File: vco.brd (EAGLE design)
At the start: 100 x 80 mm, 24 parts, among them IC2 CEM3340

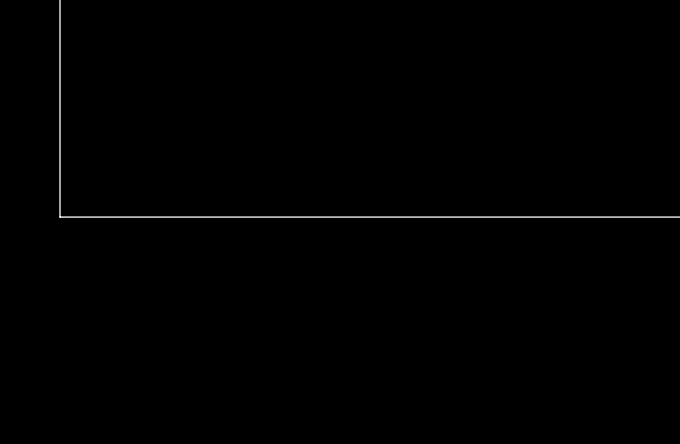
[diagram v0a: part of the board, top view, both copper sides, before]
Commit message: Added -5v regulator as option. fixed pin 4.
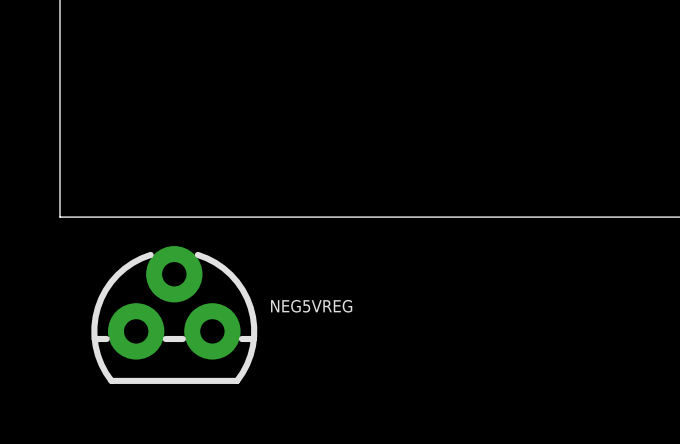
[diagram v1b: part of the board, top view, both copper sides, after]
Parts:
- added NEG5VREG: (no value), SparkFun-IC-Power:TO-92
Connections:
- removed net N$14: IC2.4, R10.1, R11.1, R12.2, R13.2, R13.3
- new net -12V: NEG5VREG.3, R10.1, R11.1, R13.2, R13.3
- new net N$18: IC2.4, R12.2
- net PE: now also NEG5VREG.2
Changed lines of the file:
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@@
 </element>
 <element name="J1" library="SparkFun-Connectors" package="2X8-SHROUDED_LOCK" value="" x="78.74" y="59.69" smashed="yes"/>
+<element name="NEG5VREG" library="SparkFun-IC-Power" package="TO-92" value="" x="3.81" y="-3.81" smashed="yes">
+<attribute name="NAME" x="6.985" y="-3.175" size="0.4064" layer="25" ratio="10"/>
+<attribute name="VALUE" x="6.985" y="-5.08" size="0.4064" layer="27" ratio="10"/>
+</element>
 </elements>
 <signals>
@@
 <contactref element="R14" pad="3"/>
 <contactref element="R12" pad="1"/>
-<wire x1="26.67" y1="36.83" x2="16.51" y2="25.4" width="0" layer="19" extent="1-1"/>
-<wire x1="33.02" y1="31.75" x2="26.67" y2="36.83" width="0" layer="19" extent="1-1"/>
-<wire x1="40.64" y1="44.45" x2="33.02" y2="31.75" width="0" layer="19" extent="1-1"/>
-<wire x1="83.82" y1="31.72" x2="26.67" y2="36.83" width="0" layer="19" extent="1-1"/>
+<contactref element="NEG5VREG" pad="2"/>
+<wire x1="40.64" y1="44.45" x2="83.82" y2="31.72" width="0" layer="19" extent="1-1"/>
+<wire x1="33.02" y1="31.75" x2="40.64" y2="44.45" width="0" layer="19" extent="1-1"/>
+<wire x1="26.67" y1="36.83" x2="33.02" y2="31.75" width="0" layer="19" extent="1-1"/>
+<wire x1="16.51" y1="25.4" x2="26.67" y2="36.83" width="0" layer="19" extent="1-1"/>
 <wire x1="34.29" y1="63.5" x2="40.64" y2="44.45" width="0" layer="19" extent="1-1"/>
-<wire x1="3.81" y1="68.58" x2="83.82" y2="31.72" width="0" layer="19" extent="1-1"/>
+<wire x1="3.81" y1="-1.905" x2="16.51" y2="25.4" width="0" layer="19" extent="1-1"/>
+<wire x1="3.81" y1="68.58" x2="34.29" y2="63.5" width="0" layer="19" extent="1-1"/>
 </signal>
 <signal name="N$10">
@@
 <contactref element="R13" pad="1"/>
 <wire x1="78.74" y1="18.99" x2="34.29" y2="68.58" width="0" layer="19" extent="1-1"/>
-</signal>
-<signal name="N$14">
-<contactref element="R13" pad="2"/>
-<contactref element="R10" pad="1"/>
-<contactref element="R13" pad="3"/>
-<contactref element="R11" pad="1"/>
-<contactref element="IC2" pad="4"/>
-<contactref element="R12" pad="2"/>
-<wire x1="83.82" y1="18.99" x2="30.48" y2="24.13" width="0" layer="19" extent="1-1"/>
-<wire x1="81.28" y1="18.99" x2="83.82" y2="18.99" width="0" layer="19" extent="1-1"/>
-<wire x1="24.13" y1="68.58" x2="81.28" y2="18.99" width="0" layer="19" extent="1-1"/>
-<wire x1="13.97" y1="68.58" x2="24.13" y2="68.58" width="0" layer="19" extent="1-1"/>
-<wire x1="11.43" y1="68.58" x2="13.97" y2="68.58" width="0" layer="19" extent="1-1"/>
 </signal>
 <signal name="N$8">
@@
 <wire x1="30.48" y1="44.45" x2="35.56" y2="31.75" width="0" layer="19" extent="1-1"/>
 </signal>
+<signal name="N$18">
+<contactref element="IC2" pad="4"/>
+<contactref element="R12" pad="2"/>
+<wire x1="30.48" y1="24.13" x2="11.43" y2="68.58" width="0" layer="19" extent="1-1"/>
+</signal>
+<signal name="-12V">
+<contactref element="R13" pad="2"/>
+<contactref element="R10" pad="1"/>
+<contactref element="R13" pad="3"/>
+<contactref element="R11" pad="1"/>
+<contactref element="NEG5VREG" pad="3"/>
+<wire x1="81.28" y1="18.99" x2="83.82" y2="18.99" width="0" layer="19" extent="1-1"/>
+<wire x1="24.13" y1="68.58" x2="81.28" y2="18.99" width="0" layer="19" extent="1-1"/>
+<wire x1="13.97" y1="68.58" x2="24.13" y2="68.58" width="0" layer="19" extent="1-1"/>
+<wire x1="5.08" y1="-3.81" x2="13.97" y2="68.58" width="0" layer="19" extent="1-1"/>
+</signal>
 </signals>

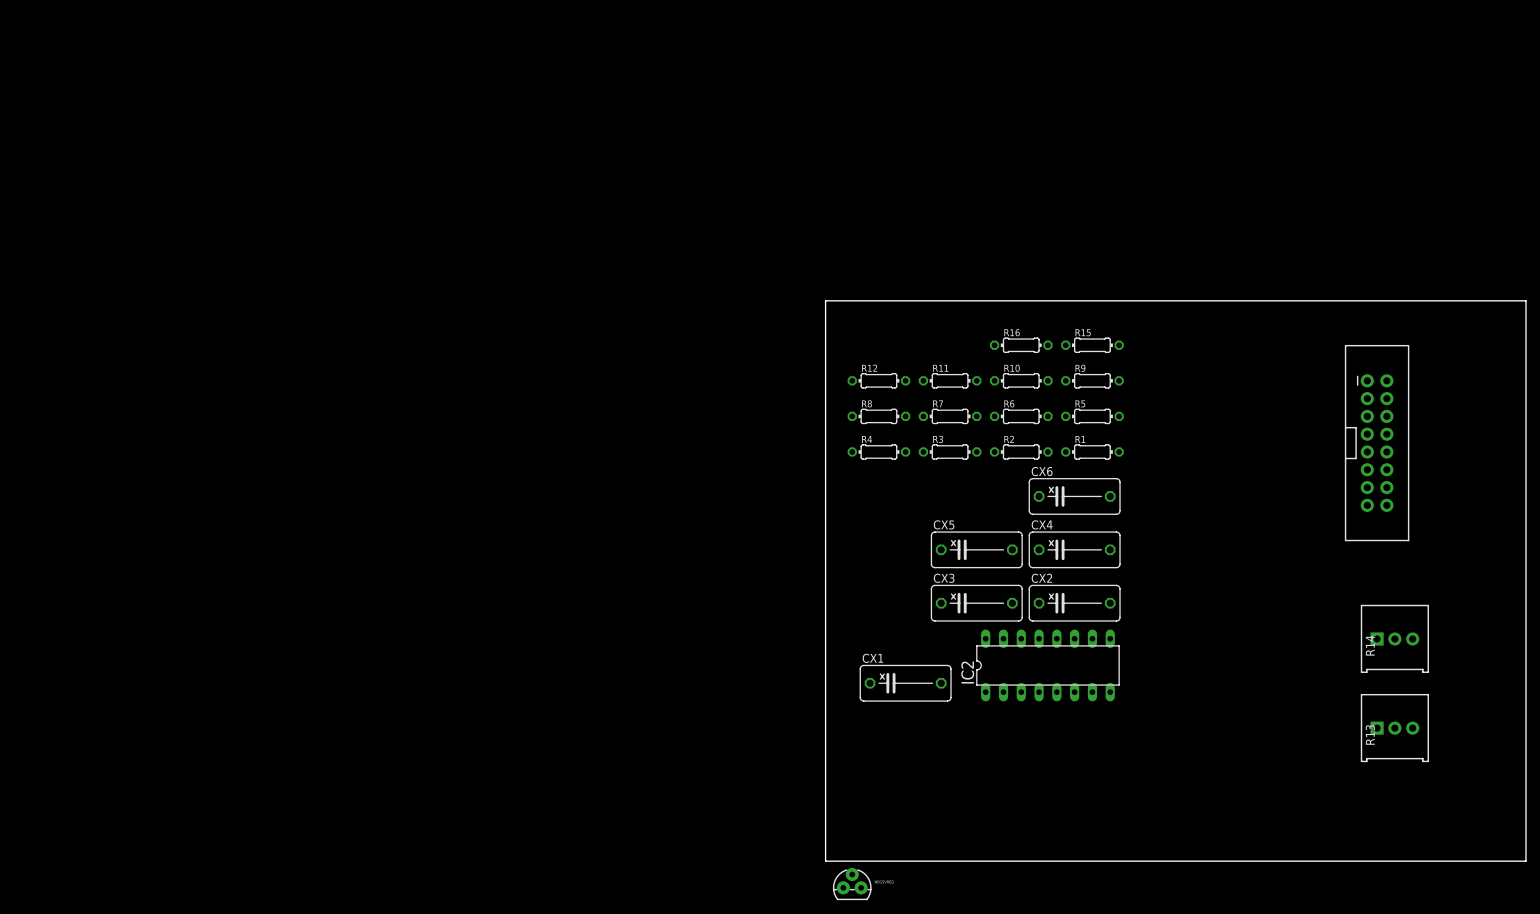
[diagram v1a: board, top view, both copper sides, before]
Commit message: Updated todo list. Updated form factors of capacitors.
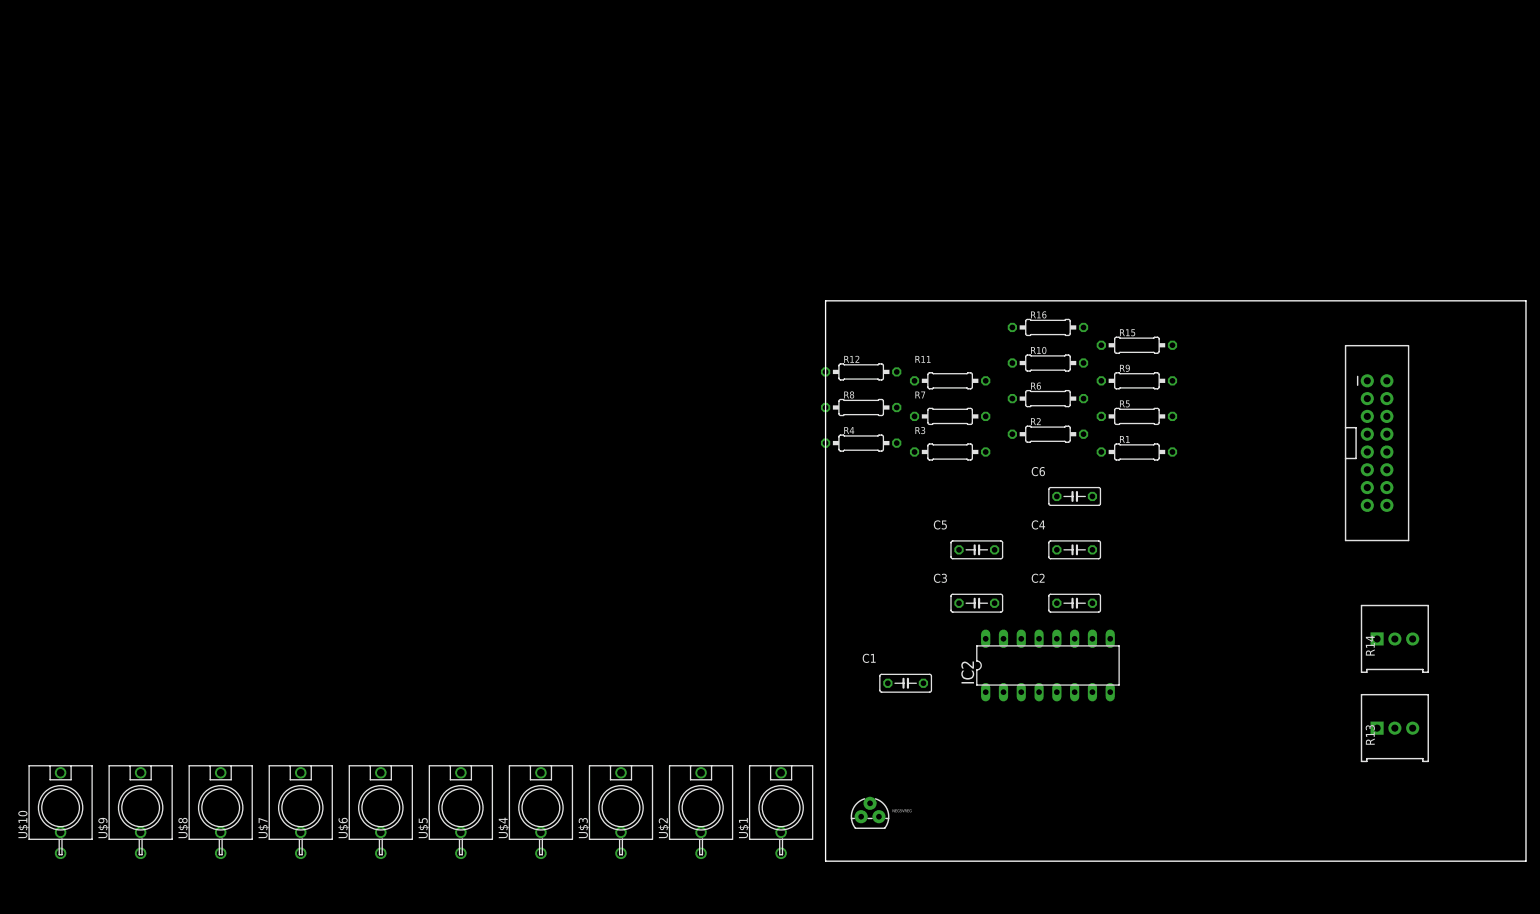
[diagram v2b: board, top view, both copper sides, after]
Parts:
- removed CX1, CX3: .01u, rcl:XC10B5
- removed CX2: .1u, rcl:XC10B5
- removed CX4: 1000p, rcl:XC10B5
- removed CX5, CX6: .001u, rcl:XC10B5
- added C1, C3: .01u, rcl:C050-025X075
- added C2: .1u, rcl:C050-025X075
- added C4: 1000p, rcl:C050-025X075
- added C5, C6: .001u, rcl:C050-025X075
- added U$1, U$10, U$2, U$3, U$4, U$5, U$6, U$7, U$8, U$9: WQP-PJ301M-12_JACK, thonkiconn:WQP-PJ301M-12_JACK
- R1, R10, R11, R12, R15, R16, R2, R3, R4, R5, R6, R7, R8, R9: device rcl:0204/7 -> rcl:0207/10
- moved NEG5VREG 10.5 mm to (6.35, 6.35)
- moved R1 6.35 mm to (44.5, 58.4)
- moved R15 6.35 mm to (44.5, 73.7)
- moved R5 6.35 mm to (44.5, 63.5)
- moved R9 6.35 mm to (44.5, 68.6)
- moved R10 4.58 mm to (31.8, 71.1)
- moved R16 4.58 mm to (31.8, 76.2)
- moved R6 4.58 mm to (31.8, 66.0)
- moved R2 4.58 mm to (31.8, 61.0)
- moved R12 2.84 mm to (5.08, 69.8)
- moved R4 2.84 mm to (5.08, 59.7)
- moved R8 2.84 mm to (5.08, 64.8)
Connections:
- new net N$14: R1.2, U$1.P$1
- new net N$19: U$1.P$2, U$1.P$3
- new net N$20: R2.1, U$2.P$1
- new net N$22: R3.1, U$3.P$1
- new net N$23: IC2.10, U$4.P$1
- new net N$24: C2.1, U$5.P$1
- new net N$25: U$2.P$2, U$2.P$3
- new net N$26: U$3.P$2, U$3.P$3
- new net N$27: U$5.P$2, U$5.P$3
- new net N$28: U$4.P$2, U$4.P$3
- new net N$29: C5.2, U$6.P$1
- new net N$30: U$6.P$2, U$6.P$3
- new net N$31: IC2.8, U$7.P$1
- new net N$32: U$7.P$2, U$7.P$3
- new net N$33: U$8.P$2, U$8.P$3
- new net N$34: C6.1, U$8.P$1
- new net N$35: IC2.5, U$9.P$1
- new net N$36: U$9.P$2, U$9.P$3
- new net N$39: U$10.P$2, U$10.P$3
- net N$12: now also NEG5VREG.1
- net N$15: now also C6.2; no longer CX6.2
- net N$18: now also U$10.P$1
- net N$2: now also C1.1; no longer CX1.1
- net N$5: now also C2.2; no longer CX2.2
- net N$6: now also C3.1; no longer CX3.1
- net N$7: now also C4.1; no longer CX4.1
- net N$9: now also C5.1; no longer CX5.1
- net PE: now also C1.2, C3.2, C4.2; no longer CX1.2, CX3.2, CX4.2

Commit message: Added a new project (version), using both sides of board.
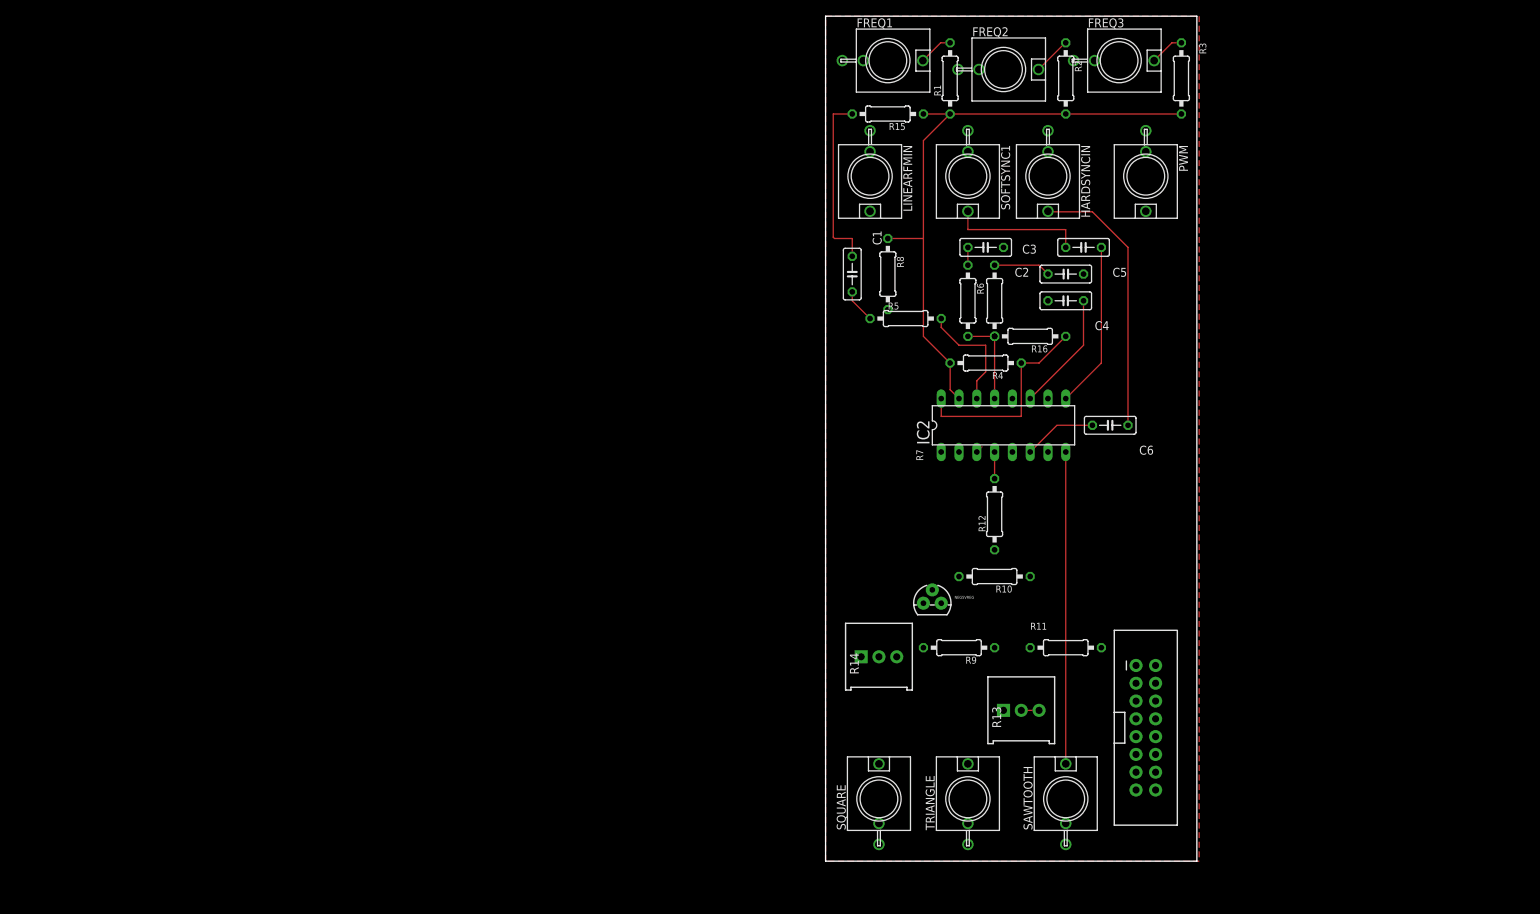
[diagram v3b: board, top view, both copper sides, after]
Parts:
- removed J1: (no value), SparkFun-Connectors:2X8-SHROUDED_LOCK
- removed U$1, U$10, U$2, U$3, U$4, U$5, U$6, U$7, U$8, U$9: WQP-PJ301M-12_JACK, thonkiconn:WQP-PJ301M-12_JACK
- added FREQ1, FREQ2, FREQ3, HARDSYNCIN, LINEARFMIN, PWM, SAWTOOTH, SOFTSYNC1, SQUARE, TRIANGLE: WQP-PJ301M-12_JACK, thonkiconn:WQP-PJ301M-12_JACK
- added J3: (no value), SparkFun-Connectors:2X8-SHROUDED_LOCK
- R8: value 10M -> 1M
- moved R14 73.7 mm to (7.62, 29.2)
- moved R3 62.7 mm to (50.8, 111.8), turned to 270 degrees
- moved R1 59.6 mm to (17.8, 111.8), turned to 90 degrees
- moved C1 58.9 mm to (3.81, 83.8), turned to 270 degrees
- moved R13 53.4 mm to (27.9, 21.5)
- moved C2 52.4 mm to (22.9, 87.6), turned to 180 degrees
- moved R2 50.9 mm to (34.3, 111.8), turned to 270 degrees
- moved C3 48.7 mm to (34.3, 83.8)
- moved R15 48.5 mm to (8.89, 106.7), turned to 180 degrees
- moved C5 45.8 mm to (36.8, 87.6), turned to 180 degrees
- moved R9 45.8 mm to (19.1, 30.5), turned to 180 degrees
- moved R11 41.5 mm to (34.3, 30.5)
- moved R5 35.9 mm to (11.4, 77.5)
- moved C4 35.6 mm to (34.3, 80.0), turned to 180 degrees
- moved IC2 34.9 mm to (25.4, 62.2)
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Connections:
- removed net N$19: U$1.P$2, U$1.P$3
- removed net N$25: U$2.P$2, U$2.P$3
- removed net N$26: U$3.P$2, U$3.P$3
- removed net N$27: U$5.P$2, U$5.P$3
- removed net N$28: U$4.P$2, U$4.P$3
- removed net N$30: U$6.P$2, U$6.P$3
- removed net N$32: U$7.P$2, U$7.P$3
- removed net N$33: U$8.P$2, U$8.P$3
- removed net N$36: U$9.P$2, U$9.P$3
- removed net N$39: U$10.P$2, U$10.P$3
- new net +5V: J3.11, J3.12
- new net CV: J3.13, J3.14
- new net GATE: J3.15, J3.16
- new net GND: C3.2, C4.2, FREQ1.P$2, FREQ1.P$3, FREQ2.P$2, FREQ2.P$3, FREQ3.P$2, FREQ3.P$3, HARDSYNCIN.P$2, HARDSYNCIN.P$3, IC2.12, J3.3, J3.4, J3.5, J3.6, J3.7, J3.8, LINEARFMIN.P$2, LINEARFMIN.P$3, NEG5VREG.2, PWM.P$2, PWM.P$3, R12.1, R14.3, SAWTOOTH.P$2, SAWTOOTH.P$3, SOFTSYNC1.P$2, SOFTSYNC1.P$3, SQUARE.P$2, SQUARE.P$3, TRIANGLE.P$2, TRIANGLE.P$3
- net +12V: now also J3.10, J3.9, R4.1
- net -12V: now also J3.1, J3.2; no longer R10.1, R13.2, R13.3
- net N$12: now also R10.1, R13.2, R13.3
- net N$14: now also FREQ1.P$1; no longer U$1.P$1
- net N$18: now also SQUARE.P$1; no longer U$10.P$1
- net N$20: now also FREQ2.P$1; no longer U$2.P$1
- net N$22: now also FREQ3.P$1; no longer U$3.P$1
- net N$23: now also TRIANGLE.P$1; no longer U$4.P$1
- net N$24: now also LINEARFMIN.P$1; no longer U$5.P$1
- net N$29: now also SOFTSYNC1.P$1; no longer U$6.P$1
- net N$31: now also SAWTOOTH.P$1; no longer U$7.P$1
- net N$34: now also HARDSYNCIN.P$1; no longer U$8.P$1
- net N$35: now also PWM.P$1; no longer U$9.P$1
- net PE: no longer C3.2, C4.2, IC2.12, NEG5VREG.2, R12.1, R14.3
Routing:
- net N$21: track 0.00 -> 86.2 mm
- net N$31: track 0.00 -> 44.5 mm
- net N$34: track 0.00 -> 39.0 mm
- net +12V: track 0.00 -> 29.5 mm
- net N$2: track 0.00 -> 25.7 mm
- net N$9: track 0.00 -> 23.7 mm
- net N$29: track 0.00 -> 19.1 mm
- net N$7: track 0.00 -> 17.1 mm
- net N$3: track 0.00 -> 16.8 mm
- net N$4: track 0.00 -> 12.7 mm
- net N$15: track 0.00 -> 10.5 mm
- net N$6: track 0.00 -> 8.15 mm
- net N$20: track 0.00 -> 5.47 mm
- net N$14: track 0.00 -> 4.94 mm
- net N$22: track 0.00 -> 4.94 mm
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- added copper zone on layer 1, net GND
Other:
- board size 100 x 80 mm -> 53 x 120.6 mm
